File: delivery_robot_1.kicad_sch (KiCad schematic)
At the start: 29 parts, among them J1 SWD, J10 Port C/D breakout, J2 Conn_01x02, J4 BOOT0 jumper, J5 Conn_01x03_Pin, J6 DRI0002 E1/M1/GND, J7 Motor1 encoder, J8 Port A breakout, J9 Port B breakout, SW1 RESET, U1 STM32F091RCTx, Y3 8MHz

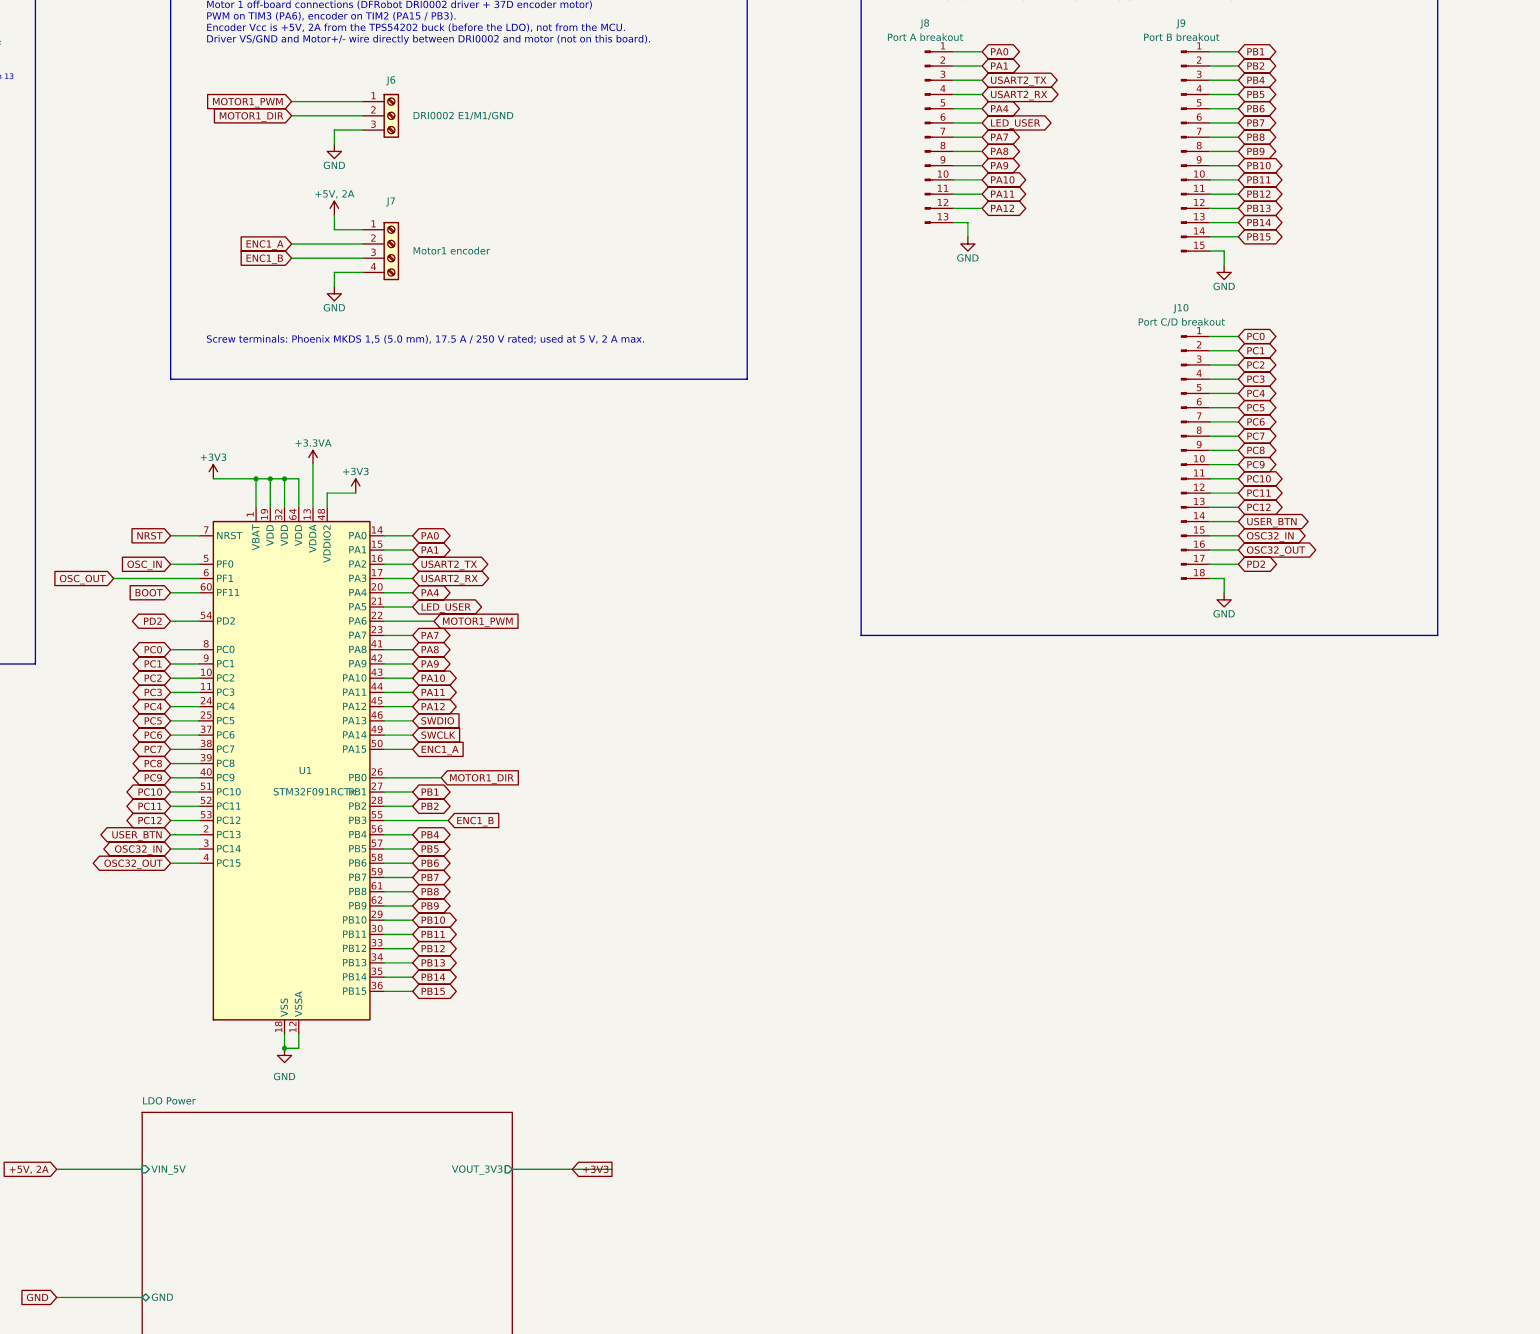
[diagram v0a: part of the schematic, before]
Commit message: Add off-board BNO085 IMU connectors on I2C1
Connect an off-board BNO085 breakout (Adafruit 4754 / SparkFun style):
- J11: JST SH 4-pin SM04B-SRSS-TB in STEMMA QT / Qwiic order
  (1 GND, 2 +3V3, 3 SDA, 4 SCL), powered from the 3.3 V LDO rail,
  mounting pads to GND
- J12: 2.54 mm 2-pin header for the IMU INT and RST lines
- R10/R11: 4.7k 0805 SDA/SCL pull-ups to +3V3, marked DNP since the
  breakout has its own

Rename the MCU global labels PB6/PB7 to IMU_SCL/IMU_SDA (I2C1, AF1)
and PC4/PC5 to IMU_INT (EXTI4)/IMU_RST. These pins remain on the J9
and J10 breakout headers, whose descriptions are updated to match.

Co-Authored-By: Claude Opus 5.5 <noreply@anthropic.com>
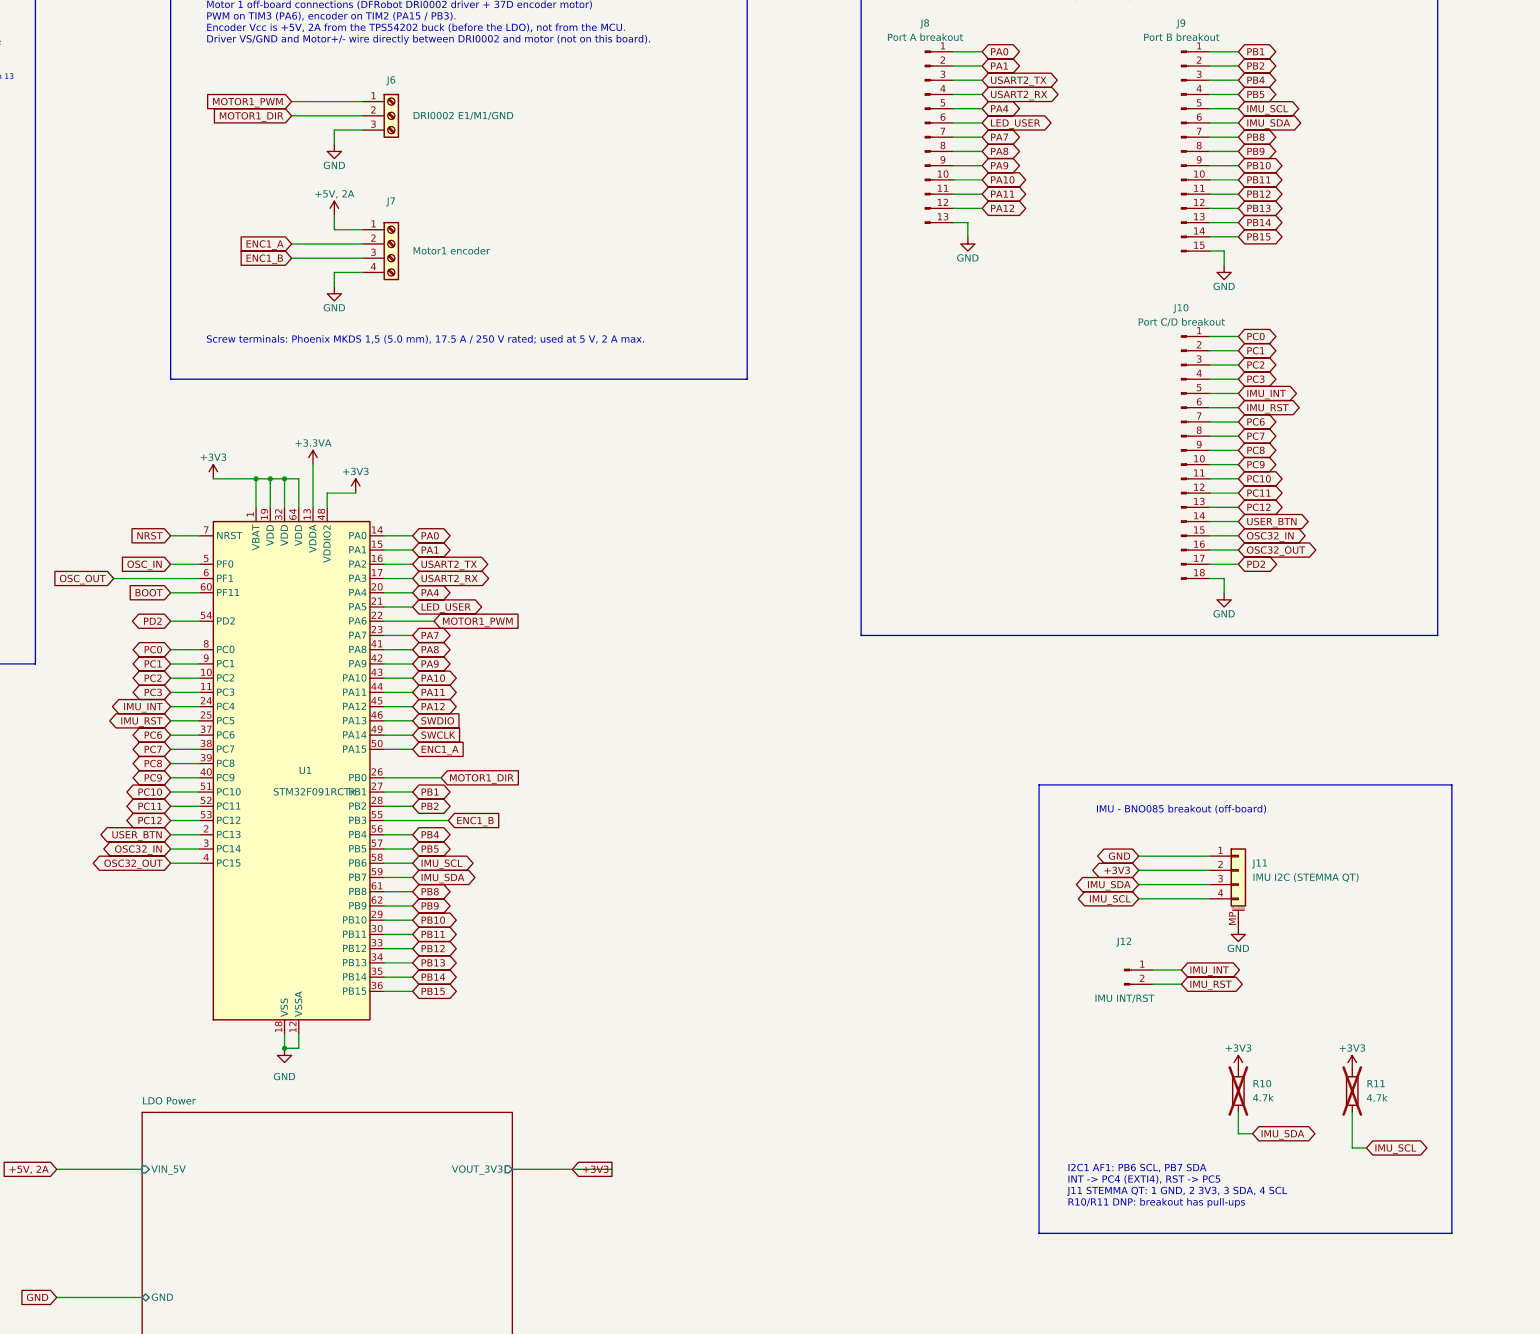
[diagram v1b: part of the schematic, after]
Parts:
- added J11: IMU I2C (STEMMA QT), Connector_JST:JST_SH_SM04B-SRSS-TB_1x04-1MP_P1.00mm_Horizontal, symbol Connector_Generic_MountingPin:Conn_01x04_MountingPin
- added J12: IMU INT/RST, Connector_PinHeader_2.54mm:PinHeader_1x02_P2.54mm_Vertical, symbol Connector:Conn_01x02_Pin
- added R10, R11: 4.7k, Resistor_SMD:R_0805_2012Metric, symbol Device:R
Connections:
- net +3V3: now also J11.2 (Pin_2), R10.1, R11.1
- net GND: now also J11.1 (Pin_1), J11.MP (MountPin)
- net PB6 renamed IMU_SCL
- net IMU_SCL: now also J11.4 (Pin_4), R11.2
- net PB7 renamed IMU_SDA
- net IMU_SDA: now also J11.3 (Pin_3), R10.2
- net PC4 renamed IMU_INT
- net IMU_INT: now also J12.1 (Pin_1)
- net PC5 renamed IMU_RST
- net IMU_RST: now also J12.2 (Pin_2)
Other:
- note added: "I2C1 AF1: PB6 SCL, PB7 SDA INT -> PC4 (EXTI4), RST -> PC5 J11 STEMMA QT: 1 GND, 2 3V3, 3 SDA, 4 SCL R10/R11 DNP: breakout has pull-ups"
- note added: "IMU - BNO085 breakout (off-board)"

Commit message: Add Raspberry Pi 5 UART screw terminal on USART2
Add a 3-wire UART link to the Pi 5 GPIO header:
- J13: Phoenix MKDS 1,5/3 5.0 mm screw terminal (1715035)
  1 = PI_TXD from Pi GPIO14 TXD (header pin 8)
  2 = PI_RXD to Pi GPIO15 RXD (header pin 10)
  3 = GND (Pi header pin 6)
- R12/R13: 100R 0805 series resistors between USART2_TX (PA2) /
  USART2_RX (PA3) and the connector lines, to place near U1

TX/RX are crossed on the board so the cable runs straight through.
Both sides use 3.3 V logic. No ESD array is fitted on these lines.

Also includes schematic layout changes made in KiCad.

Co-Authored-By: Claude Opus 5.5 <noreply@anthropic.com>
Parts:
- added J13: Pi 5 UART, TerminalBlock_Phoenix:TerminalBlock_Phoenix_MKDS-1,5-3_1x03_P5.00mm_Horizontal, symbol Connector:Screw_Terminal_01x03
- added R12, R13: 100, Resistor_SMD:R_0805_2012Metric, symbol Device:R
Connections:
- net GND: now also J13.3 (Pin_3)
- net USART2_RX: now also R13.1
- net USART2_TX: now also R12.1
- new net PI_RXD: J13.2 (Pin_2), R12.2
- new net PI_TXD: J13.1 (Pin_1), R13.2
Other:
- note added: "J13 1 <- Pi GPIO14 TXD (header pin 8) J13 2 -> Pi GPIO15 RXD (header pin 10) J13 3 = GND (Pi header pin 6); 3.3 V logic R12/R13 near U1, U5 ESD near J13"
- note added: "Raspberry Pi 5 UART (USART2, PA2 TX / PA3 RX)"
